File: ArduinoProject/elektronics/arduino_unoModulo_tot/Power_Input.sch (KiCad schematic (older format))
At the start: 8 parts, among them IC1 MC33269ST-5.OT3, U2 LP2985-3.3

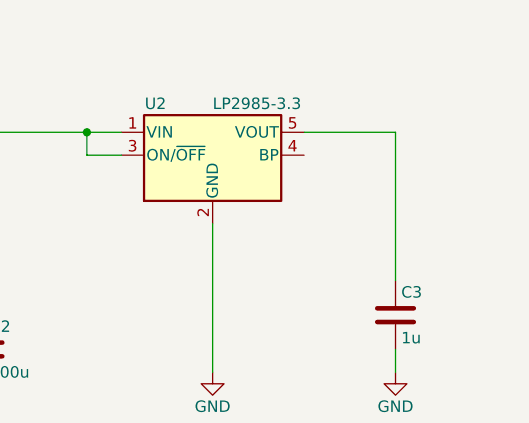
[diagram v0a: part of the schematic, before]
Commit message: kicad schema altered: alles op 1 PCB3
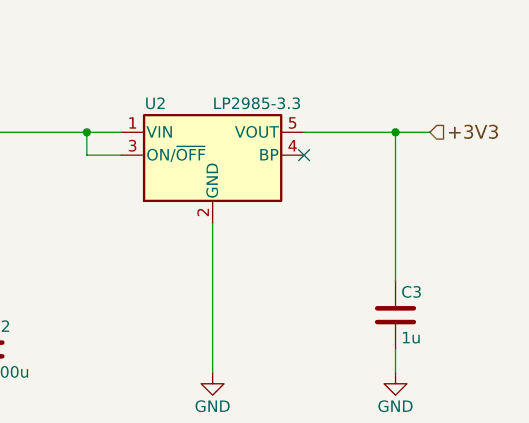
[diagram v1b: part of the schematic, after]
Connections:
- net +3V3: now reaches C3.1, U2.5 (VOUT)
- no-connect marks 0 -> 1
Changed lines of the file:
@@
 $Descr A4 11693 8268
 encoding utf-8
-Sheet 7 6
+Sheet 4 6
 Title ""
 Date ""
@@
 Connection ~ 6900 2800
 Wire Wire Line
-	7850 2800 8250 2800
+	7850 2800 8400 2800
 Wire Wire Line
 	8250 2800 8250 3450
@@
 	1    0    0    -1
 $EndComp
+NoConn ~ 7850 2900
+Connection ~ 8250 2800
+Text HLabel 8400 2800 2    60   Input ~ 0
++3V3
 $EndSCHEMATC
